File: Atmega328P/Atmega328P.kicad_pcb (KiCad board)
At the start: 4 copper layers, 50.7 x 30.7 mm, 31 parts, among them J1 Conn_01x04_Pin, J2 Conn_01x09_Pin, J3 Conn_01x04_Pin, J4 Conn_02x03_Odd_Even, U1 24LC1025, U2 DS1337S_, U3 24LC1025, U4 ATMEGA328P-AU, Y1 32.768 KHz, Y2 16 MHz

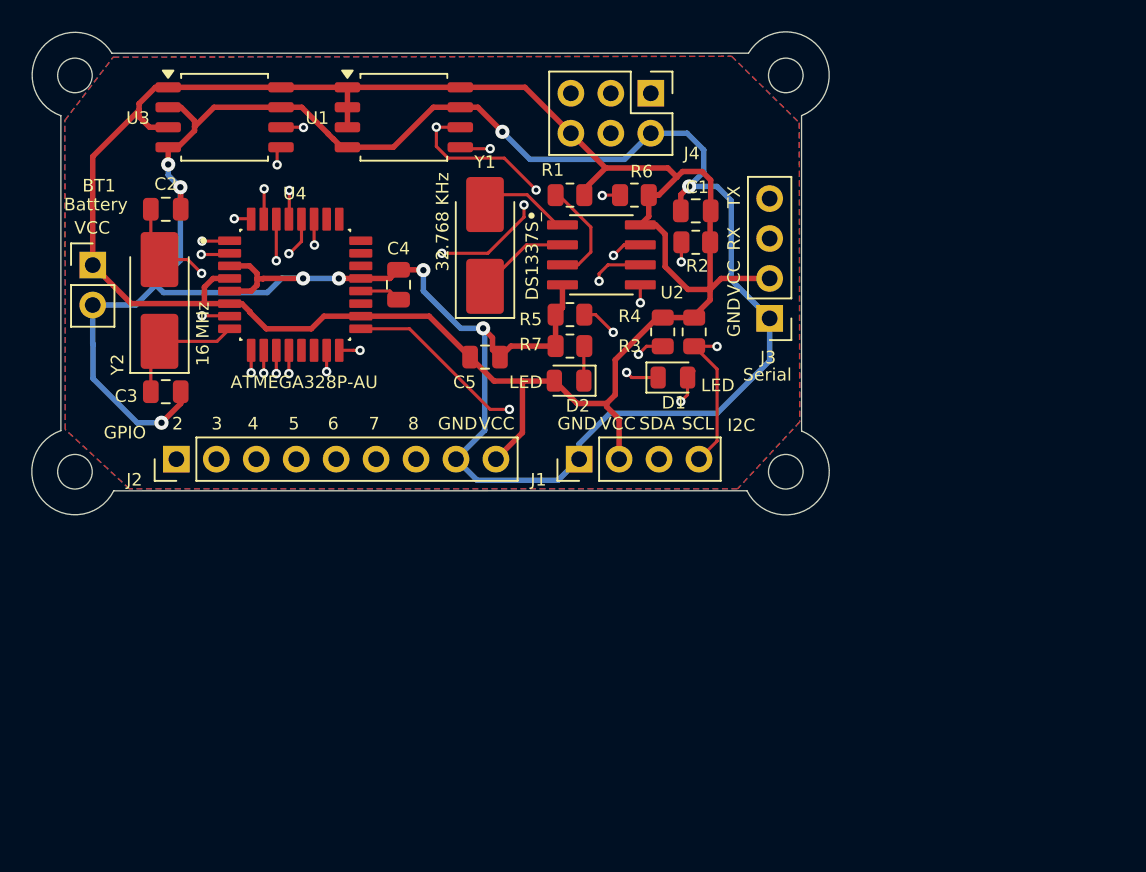
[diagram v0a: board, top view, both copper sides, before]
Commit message: completed auto routing.
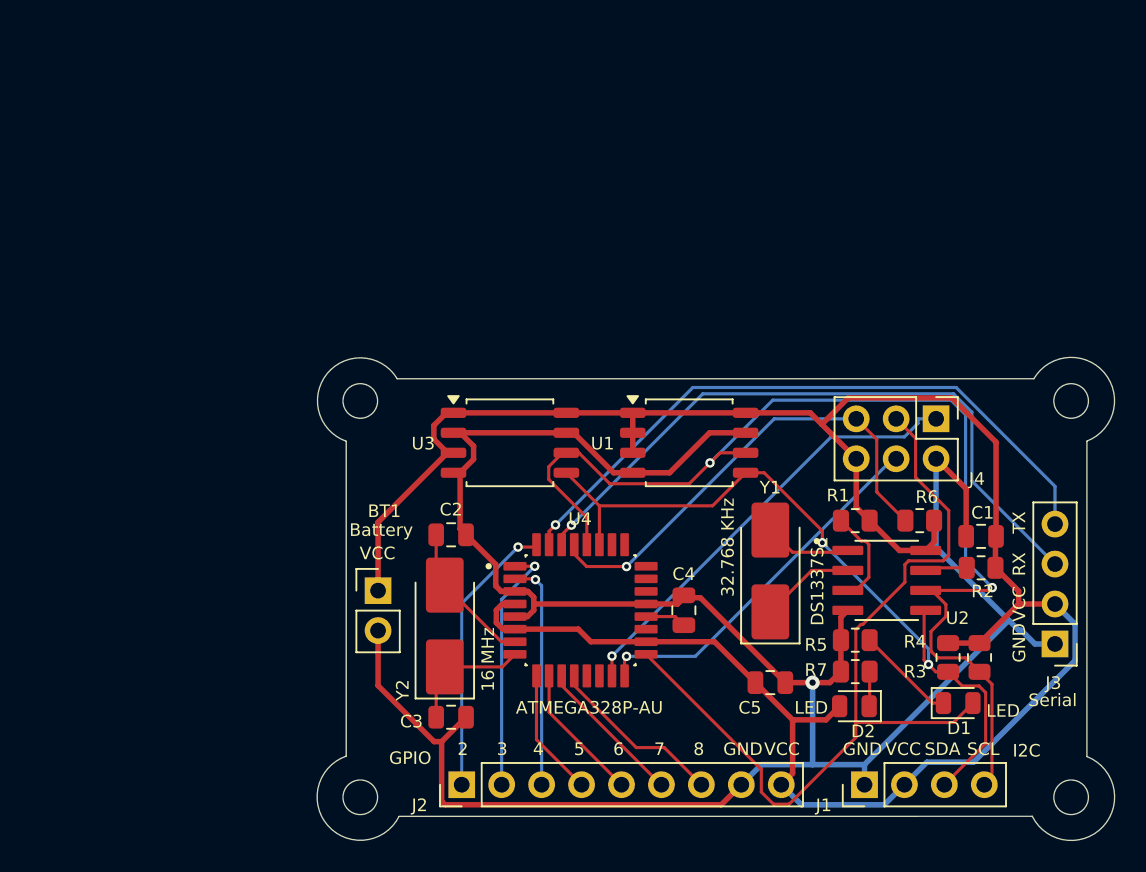
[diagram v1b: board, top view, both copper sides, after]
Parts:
- moved H1 27.5 mm to (135.6, 106.2)
- moved Y2 27.5 mm to (140.9, 120.5)
- moved BT1 27.5 mm to (136.7, 118.2)
- moved C1 27.5 mm to (175.0, 114.8)
- moved C4 27.5 mm to (156.1, 119.5)
- moved D1 27.5 mm to (173.6, 125.4)
- moved H2 27.5 mm to (180.8, 106.2)
- moved H4 27.5 mm to (135.6, 131.4)
- moved J1 27.5 mm to (167.6, 130.6)
- moved J2 27.5 mm to (142.0, 130.6)
- moved J3 27.5 mm to (179.7, 121.6)
- moved J4 27.5 mm to (172.2, 107.3)
- moved R1 27.5 mm to (167.0, 113.8)
- moved R2 27.5 mm to (175.0, 116.8)
- moved R3 27.5 mm to (172.9, 122.5)
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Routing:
- net GND: track 164.3 -> 148.3 mm, vias 9 -> 1
- net /MOSI: track 35.7 -> 28.3 mm
- net /SCL: track 64.7 -> 70.7 mm, vias 6 -> 2
- net Net-(U2-SQW/~INT): track 8.24 -> 2.68 mm, vias 2 -> 0
- net /SDA: track 52.9 -> 48.2 mm, vias 5 -> 2
- net VCC: track 141.9 -> 144.9 mm
- net /D4: track 17.0 -> 14.5 mm
- net /MISO: track 25.5 -> 23.6 mm, vias 3 -> 1
- net /SCK: track 51.6 -> 53.3 mm, vias 2 -> 0
- net Net-(U4-PB6): track 10.9 -> 9.38 mm, vias 2 -> 0
- net /TX: track 43.2 -> 41.8 mm
- net /RX: track 44.1 -> 42.8 mm
- net /D3: track 17.3 -> 16.0 mm
- net /D2: track 19.1 -> 17.8 mm
- net /D8: track 12.5 -> 11.3 mm, vias 1 -> 0
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- removed copper zone on B.Cu, net GND
- removed copper zone on F.Cu, net VCC
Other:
- copper layers 4 -> 2
